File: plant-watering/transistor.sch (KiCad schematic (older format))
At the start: 6 parts, among them Q1 BC337, Q2 BC337, Q3 BC337

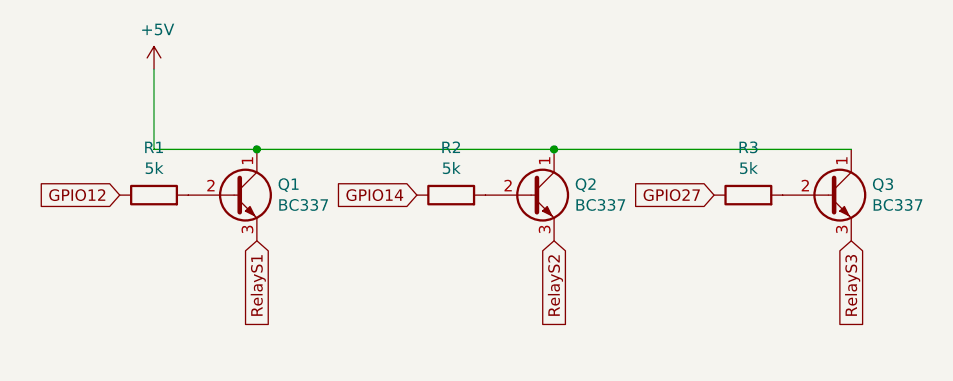
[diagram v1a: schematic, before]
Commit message: changed transistor and relay circuit
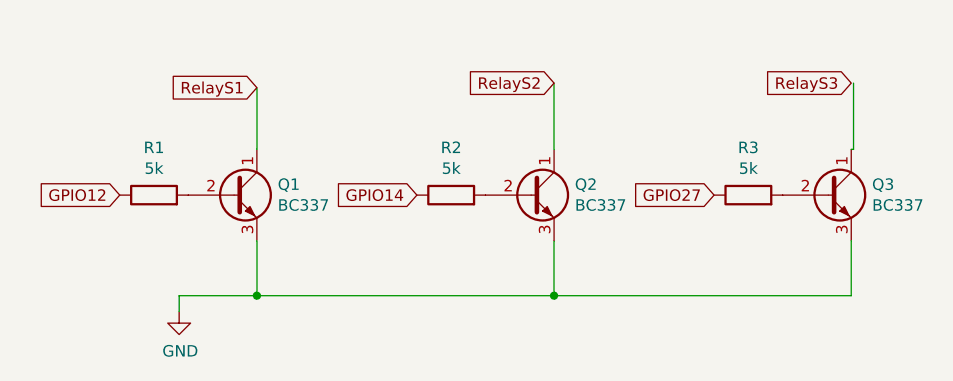
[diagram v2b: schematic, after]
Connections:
- net labels added: GND
- net labels removed: +5V
- wire segments 4 -> 11
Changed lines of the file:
@@
-	1    0    0    -1
-$EndComp
-Wire Wire Line
-	6250 3150 4950 3150
-Connection ~ 6250 3150
-Wire Wire Line
-	4950 3150 4500 3150
-Wire Wire Line
-	4500 3150 4500 2800
-Connection ~ 4950 3150
-$Comp
-L power:+5V #PWR04
-U 1 1 60099612
-P 4500 2800
-F 0 "#PWR04" H 4500 2650 50  0001 C CNN
-F 1 "+5V" H 4515 2973 50  0000 C CNN
-F 2 "" H 4500 2800 50  0001 C CNN
-F 3 "" H 4500 2800 50  0001 C CNN
-	1    4500 2800
 	1    0    0    -1
 $EndComp
@@
 Text GLabel 6950 3350 0    50   Input ~ 0
 GPIO27
+Text GLabel 4950 2880 0    50   Input ~ 0
+RelayS1
+Text GLabel 6250 2860 0    50   Input ~ 0
+RelayS2
+Text GLabel 7550 2860 0    50   Input ~ 0
+RelayS3
 Wire Wire Line
-	6250 3150 7550 3150
-Text GLabel 4950 3550 3    50   Input ~ 0
-RelayS1
-Text GLabel 6250 3550 3    50   Input ~ 0
-RelayS2
-Text GLabel 7550 3550 3    50   Input ~ 0
-RelayS3
+	7550 3550 7550 3790
+Wire Wire Line
+	4610 3790 4610 3860
+Wire Wire Line
+	4950 3550 4950 3790
+Connection ~ 4950 3790
+Wire Wire Line
+	4950 3790 4610 3790
+Wire Wire Line
+	6250 3550 6250 3790
+Wire Wire Line
+	4950 3790 6250 3790
+Connection ~ 6250 3790
+Wire Wire Line
+	6250 3790 7550 3790
+$Comp
+L power:GND #PWR?
+U 1 1 600B49D6
+P 4610 3860
+F 0 "#PWR?" H 4610 3610 50  0001 C CNN
+F 1 "GND" H 4615 3687 50  0000 C CNN
+F 2 "" H 4610 3860 50  0001 C CNN
+F 3 "" H 4610 3860 50  0001 C CNN
+	1    4610 3860
+	1    0    0    -1
+$EndComp
+Wire Wire Line
+	4950 2880 4950 3150
+Wire Wire Line
+	7560 2860 7560 3150
+Wire Wire Line
+	7560 3150 7550 3150
+Wire Wire Line
+	6250 3150 6250 2860
 $EndSCHEMATC

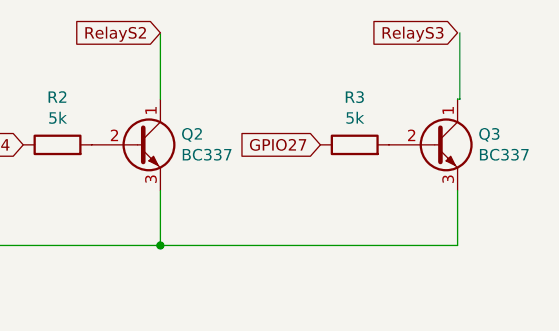
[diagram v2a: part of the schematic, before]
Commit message: edited schematic & started pcb design
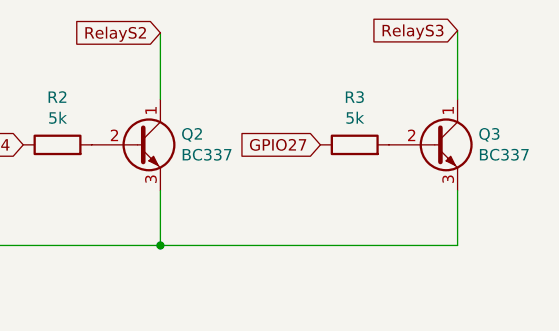
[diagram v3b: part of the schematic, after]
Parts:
- R1, R2, R3: footprint Resistors:R_Axial_DIN0204_L3.6mm_D1.6mm_P5.08mm_Vertical -> Resistors_ThroughHole:R_Axial_DIN0207_L6.3mm_D2.5mm_P5.08mm_Vertical
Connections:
- wire segments 11 -> 10
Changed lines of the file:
@@
 F 0 "R1" V 4707 3350 50  0000 C CNN
 F 1 "5k" V 4616 3350 50  0000 C CNN
-F 2 "Resistors:R_Axial_DIN0204_L3.6mm_D1.6mm_P5.08mm_Vertical" V 4430 3350 50  0001 C CNN
+F 2 "Resistors_ThroughHole:R_Axial_DIN0207_L6.3mm_D2.5mm_P5.08mm_Vertical" V 4430 3350 50  0001 C CNN
 F 3 "~" H 4500 3350 50  0001 C CNN
 	1    4500 3350
@@
 F 0 "R2" V 6007 3350 50  0000 C CNN
 F 1 "5k" V 5916 3350 50  0000 C CNN
-F 2 "Resistors:R_Axial_DIN0204_L3.6mm_D1.6mm_P5.08mm_Vertical" V 5730 3350 50  0001 C CNN
+F 2 "Resistors_ThroughHole:R_Axial_DIN0207_L6.3mm_D2.5mm_P5.08mm_Vertical" V 5730 3350 50  0001 C CNN
 F 3 "~" H 5800 3350 50  0001 C CNN
 	1    5800 3350
@@
 F 0 "R3" V 7307 3350 50  0000 C CNN
 F 1 "5k" V 7216 3350 50  0000 C CNN
-F 2 "Resistors:R_Axial_DIN0204_L3.6mm_D1.6mm_P5.08mm_Vertical" V 7030 3350 50  0001 C CNN
+F 2 "Resistors_ThroughHole:R_Axial_DIN0207_L6.3mm_D2.5mm_P5.08mm_Vertical" V 7030 3350 50  0001 C CNN
 F 3 "~" H 7100 3350 50  0001 C CNN
 	1    7100 3350
@@
 Text GLabel 6250 2860 0    50   Input ~ 0
 RelayS2
-Text GLabel 7550 2860 0    50   Input ~ 0
+Text GLabel 7550 2850 0    50   Input ~ 0
 RelayS3
 Wire Wire Line
@@
 	6250 3790 7550 3790
 $Comp
-L power:GND #PWR?
+L power:GND #PWR0105
 U 1 1 600B49D6
 P 4610 3860
-F 0 "#PWR?" H 4610 3610 50  0001 C CNN
+F 0 "#PWR0105" H 4610 3610 50  0001 C CNN
 F 1 "GND" H 4615 3687 50  0000 C CNN
 F 2 "" H 4610 3860 50  0001 C CNN
@@
 	4950 2880 4950 3150
 Wire Wire Line
-	7560 2860 7560 3150
+	6250 3150 6250 2860
 Wire Wire Line
-	7560 3150 7550 3150
-Wire Wire Line
-	6250 3150 6250 2860
+	7550 2850 7550 3150
 $EndSCHEMATC

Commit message: added several parts#
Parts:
- added Q4, Q5, Q6: BC337, TO_SOT_Packages_THT:TO-92_Inline_Wide, symbol Transistor_BJT:BC337
- added R4, R5, R6: 5k, Resistors_ThroughHole:R_Axial_DIN0207_L6.3mm_D2.5mm_P5.08mm_Vertical, symbol Device:R
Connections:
- net GND: now also Q4.3 (E), Q5.3 (E), Q6.3 (E)
- net GPIO14 renamed GPIO13
- net GPIO27 renamed GPIO17
- new net: Q5.2 (B), R5.2
- new net: Q4.2 (B), R4.2
- new net: Q6.2 (B), R6.2
- new net GPIO16: R4.1
- new net GPIO21: R6.1
- new net GPIO22: R5.1
- new net RelayS4: Q4.1 (C)
- new net RelayS5: Q5.1 (C)
- new net RelayS6: Q6.1 (C)
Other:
- moved on the sheet: Q1, Q2, Q3, R1, R2, R3
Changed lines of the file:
@@
 $Descr A4 11693 8268
 encoding utf-8
-Sheet 2 6
+Sheet 2 7
 Title ""
 Date ""
@@
 L Transistor_BJT:BC337 Q2
 U 1 1 600920C5
-P 6150 3350
-F 0 "Q2" H 6341 3396 50  0000 L CNN
-F 1 "BC337" H 6341 3305 50  0000 L CNN
-F 2 "TO_SOT_Packages_THT:TO-92_Inline_Wide" H 6350 3275 50  0001 L CIN
-F 3 "https://diotec.com/tl_files/diotec/files/pdf/datasheets/bc337.pdf" H 6150 3350 50  0001 L CNN
-	1    6150 3350
+P 5600 3570
+F 0 "Q2" H 5791 3616 50  0000 L CNN
+F 1 "BC337" H 5791 3525 50  0000 L CNN
+F 2 "TO_SOT_Packages_THT:TO-92_Inline_Wide" H 5800 3495 50  0001 L CIN
+F 3 "https://diotec.com/tl_files/diotec/files/pdf/datasheets/bc337.pdf" H 5600 3570 50  0001 L CNN
+	1    5600 3570
 	1    0    0    -1
 $EndComp
@@
 L Transistor_BJT:BC337 Q1
 U 1 1 60094894
-P 4850 3350
-F 0 "Q1" H 5041 3396 50  0000 L CNN
-F 1 "BC337" H 5041 3305 50  0000 L CNN
-F 2 "TO_SOT_Packages_THT:TO-92_Inline_Wide" H 5050 3275 50  0001 L CIN
-F 3 "https://diotec.com/tl_files/diotec/files/pdf/datasheets/bc337.pdf" H 4850 3350 50  0001 L CNN
-	1    4850 3350
+P 4300 3570
+F 0 "Q1" H 4491 3616 50  0000 L CNN
+F 1 "BC337" H 4491 3525 50  0000 L CNN
+F 2 "TO_SOT_Packages_THT:TO-92_Inline_Wide" H 4500 3495 50  0001 L CIN
+F 3 "https://diotec.com/tl_files/diotec/files/pdf/datasheets/bc337.pdf" H 4300 3570 50  0001 L CNN
+	1    4300 3570
 	1    0    0    -1
 $EndComp
@@
 L Transistor_BJT:BC337 Q3
 U 1 1 60097816
-P 7450 3350
-F 0 "Q3" H 7641 3396 50  0000 L CNN
-F 1 "BC337" H 7641 3305 50  0000 L CNN
-F 2 "TO_SOT_Packages_THT:TO-92_Inline_Wide" H 7650 3275 50  0001 L CIN
-F 3 "https://diotec.com/tl_files/diotec/files/pdf/datasheets/bc337.pdf" H 7450 3350 50  0001 L CNN
-	1    7450 3350
+P 6900 3570
+F 0 "Q3" H 7091 3616 50  0000 L CNN
+F 1 "BC337" H 7091 3525 50  0000 L CNN
+F 2 "TO_SOT_Packages_THT:TO-92_Inline_Wide" H 7100 3495 50  0001 L CIN
+F 3 "https://diotec.com/tl_files/diotec/files/pdf/datasheets/bc337.pdf" H 6900 3570 50  0001 L CNN
+	1    6900 3570
 	1    0    0    -1
 $EndComp
@@
 L Device:R R1
 U 1 1 600997DD
-P 4500 3350
-F 0 "R1" V 4707 3350 50  0000 C CNN
-F 1 "5k" V 4616 3350 50  0000 C CNN
-F 2 "Resistors_ThroughHole:R_Axial_DIN0207_L6.3mm_D2.5mm_P5.08mm_Vertical" V 4430 3350 50  0001 C CNN
-F 3 "~" H 4500 3350 50  0001 C CNN
-	1    4500 3350
+P 3950 3570
+F 0 "R1" V 4157 3570 50  0000 C CNN
+F 1 "5k" V 4066 3570 50  0000 C CNN
+F 2 "Resistors_ThroughHole:R_Axial_DIN0207_L6.3mm_D2.5mm_P5.08mm_Vertical" V 3880 3570 50  0001 C CNN
+F 3 "~" H 3950 3570 50  0001 C CNN
+	1    3950 3570
 	0    -1   -1   0
 $EndComp
@@
 L Device:R R2
 U 1 1 6009B0BD
-P 5800 3350
-F 0 "R2" V 6007 3350 50  0000 C CNN
-F 1 "5k" V 5916 3350 50  0000 C CNN
-F 2 "Resistors_ThroughHole:R_Axial_DIN0207_L6.3mm_D2.5mm_P5.08mm_Vertical" V 5730 3350 50  0001 C CNN
-F 3 "~" H 5800 3350 50  0001 C CNN
-	1    5800 3350
+P 5250 3570
+F 0 "R2" V 5457 3570 50  0000 C CNN
+F 1 "5k" V 5366 3570 50  0000 C CNN
+F 2 "Resistors_ThroughHole:R_Axial_DIN0207_L6.3mm_D2.5mm_P5.08mm_Vertical" V 5180 3570 50  0001 C CNN
+F 3 "~" H 5250 3570 50  0001 C CNN
+	1    5250 3570
 	0    -1   -1   0
 $EndComp
@@
 L Device:R R3
 U 1 1 6009B7E0
-P 7100 3350
-F 0 "R3" V 7307 3350 50  0000 C CNN
-F 1 "5k" V 7216 3350 50  0000 C CNN
-F 2 "Resistors_ThroughHole:R_Axial_DIN0207_L6.3mm_D2.5mm_P5.08mm_Vertical" V 7030 3350 50  0001 C CNN
-F 3 "~" H 7100 3350 50  0001 C CNN
-	1    7100 3350
-	0    -1   -1   0
-$EndComp
-Text GLabel 4350 3350 0    50   Input ~ 0
+P 6550 3570
+F 0 "R3" V 6757 3570 50  0000 C CNN
+F 1 "5k" V 6666 3570 50  0000 C CNN
+F 2 "Resistors_ThroughHole:R_Axial_DIN0207_L6.3mm_D2.5mm_P5.08mm_Vertical" V 6480 3570 50  0001 C CNN
+F 3 "~" H 6550 3570 50  0001 C CNN
+	1    6550 3570
+	0    -1   -1   0
+$EndComp
+Text GLabel 3800 3570 0    50   Input ~ 0
 GPIO12
-Text GLabel 5650 3350 0    50   Input ~ 0
-GPIO14
-Text GLabel 6950 3350 0    50   Input ~ 0
-GPIO27
-Text GLabel 4950 2880 0    50   Input ~ 0
+Text GLabel 5100 3570 0    50   Input ~ 0
+GPIO13
+Text GLabel 6400 3570 0    50   Input ~ 0
+GPIO17
+Text GLabel 4400 3100 0    50   Input ~ 0
 RelayS1
-Text GLabel 6250 2860 0    50   Input ~ 0
+Text GLabel 5700 3080 0    50   Input ~ 0
 RelayS2
-Text GLabel 7550 2850 0    50   Input ~ 0
+Text GLabel 7000 3070 0    50   Input ~ 0
 RelayS3
 Wire Wire Line
-	7550 3550 7550 3790
-Wire Wire Line
-	4610 3790 4610 3860
-Wire Wire Line
-	4950 3550 4950 3790
-Connection ~ 4950 3790
-Wire Wire Line
-	4950 3790 4610 3790
-Wire Wire Line
-	6250 3550 6250 3790
-Wire Wire Line
-	4950 3790 6250 3790
-Connection ~ 6250 3790
-Wire Wire Line
-	6250 3790 7550 3790
+	7000 3770 7000 4010
+Wire Wire Line
+	4060 4010 4060 4080
+Wire Wire Line
+	4400 3770 4400 4010
+Connection ~ 4400 4010
+Wire Wire Line
+	4400 4010 4060 4010
+Wire Wire Line
+	5700 3770 5700 4010
+Wire Wire Line
+	4400 4010 5700 4010
+Connection ~ 5700 4010
+Wire Wire Line
+	5700 4010 7000 4010
 $Comp
 L power:GND #PWR0105
 U 1 1 600B49D6
-P 4610 3860
-F 0 "#PWR0105" H 4610 3610 50  0001 C CNN
-F 1 "GND" H 4615 3687 50  0000 C CNN
-F 2 "" H 4610 3860 50  0001 C CNN
-F 3 "" H 4610 3860 50  0001 C CNN
-	1    4610 3860
-	1    0    0    -1
-$EndComp
-Wire Wire Line
-	4950 2880 4950 3150
-Wire Wire Line
-	6250 3150 6250 2860
-Wire Wire Line
-	7550 2850 7550 3150
+P 4060 4080
+F 0 "#PWR0105" H 4060 3830 50  0001 C CNN
+F 1 "GND" H 4065 3907 50  0000 C CNN
+F 2 "" H 4060 4080 50  0001 C CNN
+F 3 "" H 4060 4080 50  0001 C CNN
+	1    4060 4080
+	1    0    0    -1
+$EndComp
+Wire Wire Line
+	4400 3100 4400 3370
+Wire Wire Line
+	5700 3370 5700 3080
+Wire Wire Line
+	7000 3070 7000 3370
+$Comp
+L Transistor_BJT:BC337 Q5
+U 1 1 600EAB81
+P 5600 4960
+F 0 "Q5" H 5791 5006 50  0000 L CNN
+F 1 "BC337" H 5791 4915 50  0000 L CNN
+F 2 "TO_SOT_Packages_THT:TO-92_Inline_Wide" H 5800 4885 50  0001 L CIN
+F 3 "https://diotec.com/tl_files/diotec/files/pdf/datasheets/bc337.pdf" H 5600 4960 50  0001 L CNN
+	1    5600 4960
+	1    0    0    -1
+$EndComp
+$Comp
+L Transistor_BJT:BC337 Q4
+U 1 1 600EAB87
+P 4300 4960
+F 0 "Q4" H 4491 5006 50  0000 L CNN
+F 1 "BC337" H 4491 4915 50  0000 L CNN
+F 2 "TO_SOT_Packages_THT:TO-92_Inline_Wide" H 4500 4885 50  0001 L CIN
+F 3 "https://diotec.com/tl_files/diotec/files/pdf/datasheets/bc337.pdf" H 4300 4960 50  0001 L CNN
+	1    4300 4960
+	1    0    0    -1
+$EndComp
+$Comp
+L Transistor_BJT:BC337 Q6
+U 1 1 600EAB8D
+P 6900 4960
+F 0 "Q6" H 7091 5006 50  0000 L CNN
+F 1 "BC337" H 7091 4915 50  0000 L CNN
+F 2 "TO_SOT_Packages_THT:TO-92_Inline_Wide" H 7100 4885 50  0001 L CIN
+F 3 "https://diotec.com/tl_files/diotec/files/pdf/datasheets/bc337.pdf" H 6900 4960 50  0001 L CNN
+	1    6900 4960
+	1    0    0    -1
+$EndComp
+$Comp
+L Device:R R4
+U 1 1 600EAB93
+P 3950 4960
+F 0 "R4" V 4157 4960 50  0000 C CNN
+F 1 "5k" V 4066 4960 50  0000 C CNN
+F 2 "Resistors_ThroughHole:R_Axial_DIN0207_L6.3mm_D2.5mm_P5.08mm_Vertical" V 3880 4960 50  0001 C CNN
+F 3 "~" H 3950 4960 50  0001 C CNN
+	1    3950 4960
+	0    -1   -1   0
+$EndComp
+$Comp
+L Device:R R5
+U 1 1 600EAB99
+P 5250 4960
+F 0 "R5" V 5457 4960 50  0000 C CNN
+F 1 "5k" V 5366 4960 50  0000 C CNN
+F 2 "Resistors_ThroughHole:R_Axial_DIN0207_L6.3mm_D2.5mm_P5.08mm_Vertical" V 5180 4960 50  0001 C CNN
+F 3 "~" H 5250 4960 50  0001 C CNN
+	1    5250 4960
+	0    -1   -1   0
+$EndComp
+$Comp
+L Device:R R6
+U 1 1 600EAB9F
+P 6550 4960
+F 0 "R6" V 6757 4960 50  0000 C CNN
+F 1 "5k" V 6666 4960 50  0000 C CNN
+F 2 "Resistors_ThroughHole:R_Axial_DIN0207_L6.3mm_D2.5mm_P5.08mm_Vertical" V 6480 4960 50  0001 C CNN
+F 3 "~" H 6550 4960 50  0001 C CNN
+	1    6550 4960
+	0    -1   -1   0
+$EndComp
+Text GLabel 4400 4490 0    50   Input ~ 0
+RelayS4
+Text GLabel 5700 4470 0    50   Input ~ 0
+RelayS5
+Text GLabel 7000 4460 0    50   Input ~ 0
+RelayS6
+Wire Wire Line
+	7000 5160 7000 5400
+Wire Wire Line
+	4400 5160 4400 5400
+Wire Wire Line
+	5700 5160 5700 5400
+Wire Wire Line
+	4400 5400 5700 5400
+Connection ~ 5700 5400
+Wire Wire Line
+	5700 5400 7000 5400
+Wire Wire Line
+	4400 4490 4400 4760
+Wire Wire Line
+	5700 4760 5700 4470
+Wire Wire Line
+	7000 4460 7000 4760
+Wire Wire Line
+	4400 5400 4060 5400
+Wire Wire Line
+	4060 5400 4060 5500
+Connection ~ 4400 5400
+$Comp
+L power:GND #PWR0108
+U 1 1 601385D8
+P 4060 5500
+F 0 "#PWR0108" H 4060 5250 50  0001 C CNN
+F 1 "GND" H 4065 5327 50  0000 C CNN
+F 2 "" H 4060 5500 50  0001 C CNN
+F 3 "" H 4060 5500 50  0001 C CNN
+	1    4060 5500
+	1    0    0    -1
+$EndComp
+Text GLabel 3800 4960 0    50   Input ~ 0
+GPIO16
+Text GLabel 5100 4960 0    50   Input ~ 0
+GPIO22
+Text GLabel 6400 4960 0    50   Input ~ 0
+GPIO21
 $EndSCHEMATC
